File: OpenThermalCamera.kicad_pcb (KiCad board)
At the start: 2 copper layers, 26 x 20 mm, 23 parts, among them J1 Conn_ARM_JTAG_SWD_10, J2 DX07P024AJ1R1500, SW1 PB_Bootloader, U1 MLX90640, U2 TPS793333-EP, U3 STM32F042F6Px, U4 NUP2202

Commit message: First Rev3-C commit
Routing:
- net GND: track 82.0 -> 87.8 mm, vias 12 -> 14
- net +5V: track 46.0 -> 44.9 mm
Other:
- board text added: "OTC Rev3-C"
- board text removed: "OTC Rev3"

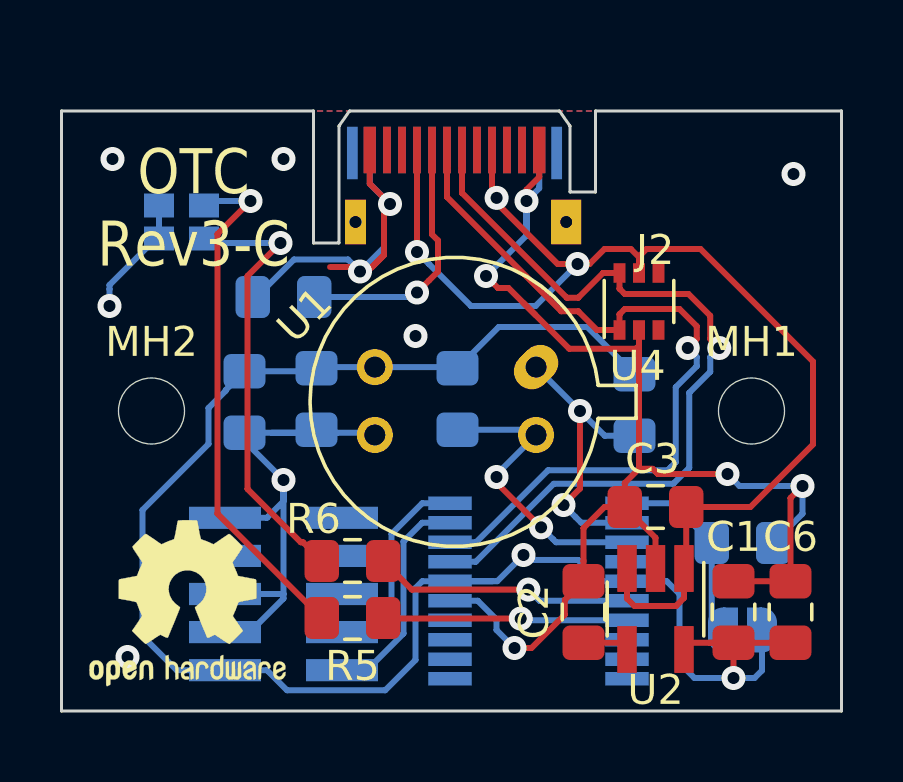
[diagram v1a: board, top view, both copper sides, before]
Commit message: Fixed reversible microusb footprint
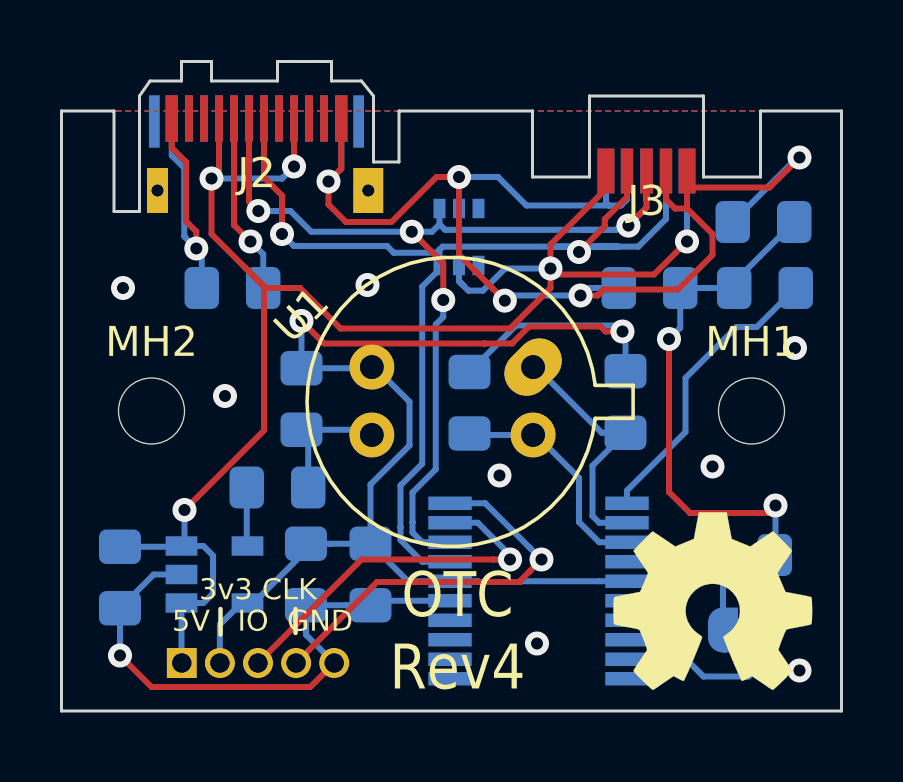
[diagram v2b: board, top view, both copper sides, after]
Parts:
- removed D1: LED_Dual_ACAC, LED_SMD:LED_Cree-PLCC4_2x2mm_CW
- added J3: micro5p_reversible, lib_fp:micro5p_reversible_edley_technology, F.Cu at (46.5, 28.0)
- C1, C2, C3, C6, U4: moved to B.Cu
- C4: value 1uF -> 10uF
- G1: value (none) -> Logo_Open_Hardware_Small; footprint Symbol:OSHW-Logo2_7.3x6mm_SilkScreen -> Symbol:OSHW-Symbol_6.7x6mm_SilkScreen
- J1: value Conn_ARM_JTAG_SWD_10 -> Conn_01x05_Female; footprint Connector_PinHeader_1.27mm:PinHeader_2x05_P1.27mm_Vertical_SMD -> Connector_PinHeader_1.27mm:PinHeader_1x05_P1.27mm_Vertical
- R1: value 10k -> 50k
- R5: value 10R -> 1k; moved to B.Cu
- R6: value 130R -> 1k; moved to B.Cu
- U2: value TPS793333-EP -> TPS79333-EP; footprint Package_TO_SOT_SMD:SOT-23-5_HandSoldering -> Package_TO_SOT_SMD:SOT-23-5; moved to B.Cu
- moved C3 18.0 mm to (28.9, 42.5), turned to 270 degrees
- moved R5 17.6 mm to (50.5, 32.9)
- moved G1 17.5 mm to (48.7, 43.4)
- moved U2 14.7 mm to (32.1, 42.5), turned to 0 degrees
- moved C1 14.3 mm to (35.1, 42.5), turned to 270 degrees
- moved C6 14.1 mm to (37.3, 42.5), turned to 270 degrees
- moved R6 13.1 mm to (49.8, 41.8)
- moved C4 11.7 mm to (46.6, 32.9), turned to 180 degrees
- moved C2 11.0 mm to (34.2, 39.5), turned to 0 degrees
- moved R1 10.7 mm to (50.4, 30.7), turned to 180 degrees
- moved J2 6.68 mm to (33.8, 28.4)
- moved U4 6.37 mm to (40.2, 31.2), turned to 270 degrees
- moved J1 4.10 mm to (31.0, 45.4), turned to 270 degrees
- moved C5 1.90 mm to (35.0, 36.6)
- moved R4 1.73 mm to (32.7, 32.9)
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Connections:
- C4 pad 1: +3V3 -> Net-(C4-Pad1)
- J1 pad 1: +3V3 -> +5V
- J1 pad 2: /SWDIO -> +3V3
- J1 pad 3: GND -> /SWDIO
- J2 pad A10: Net-(J2-PadA10) -> (no net)
- J2 pad A11: Net-(J2-PadA11) -> (no net)
- J2 pad A2: Net-(J2-PadA2) -> (no net)
- J2 pad A3: Net-(J2-PadA3) -> (no net)
- J2 pad A8: Net-(J2-PadA8) -> (no net)
- J2 pad B10: Net-(J2-PadB10) -> (no net)
- J2 pad B11: Net-(J2-PadB11) -> (no net)
- J2 pad B2: Net-(J2-PadB2) -> (no net)
- J2 pad B3: Net-(J2-PadB3) -> (no net)
- J2 pad B5: Net-(J2-PadB5) -> (no net)
- J2 pad B8: Net-(J2-PadB8) -> (no net)
- R1 pad 1: /BOOT0 -> Net-(C4-Pad1)
- R5 pad 1: Net-(D1-Pad1) -> Net-(C4-Pad1)
- R5 pad 2: /RED_LED -> /BOOT0
- R6 pad 1: /BLUE_LED -> Net-(C4-Pad1)
- R6 pad 2: Net-(D1-Pad4) -> Net-(R6-Pad2)
- SW1 pad 1: /BOOT0 -> Net-(R6-Pad2)
- U3 pad 10: Net-(U3-Pad10) -> (no net)
- U3 pad 11: Net-(U3-Pad11) -> (no net)
- U3 pad 12: Net-(U3-Pad12) -> (no net)
- U3 pad 13: Net-(U3-Pad13) -> (no net)
- U3 pad 14: Net-(U3-Pad14) -> (no net)
- U3 pad 4: Net-(U3-Pad4) -> (no net)
- U3 pad 6: /BLUE_LED -> (no net)
- U3 pad 7: /RED_LED -> (no net)
- U3 pad 8: Net-(U3-Pad8) -> (no net)
- U3 pad 9: Net-(U3-Pad9) -> (no net)
- U4 pad 3: Net-(U4-Pad3) -> (no net)
- U4 pad 4: Net-(U4-Pad4) -> (no net)
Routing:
- net Net-(D1-Pad1): track 17.4 -> 0.00 mm, vias 1 -> 0
- net Net-(C4-Pad1): track 0.00 -> 17.4 mm, vias 0 -> 2
- net +5V: track 44.9 -> 61.1 mm, vias 3 -> 5
- net Net-(D1-Pad4): track 14.7 -> 0.00 mm, vias 1 -> 0
- net /USB_N: track 27.9 -> 38.4 mm, vias 1 -> 2
- net /BLUE_LED: track 8.67 -> 0.00 mm, vias 1 -> 0
- net /USB_P: track 26.3 -> 34.7 mm, vias 1 -> 4
- net /RED_LED: track 8.16 -> 0.00 mm, vias 1 -> 0
- net +3V3: track 60.8 -> 54.1 mm
- net /SWDCLK: track 6.81 -> 13.4 mm, vias 0 -> 1
- net GND: track 87.8 -> 82.6 mm, vias 14 -> 15
- net /SWDIO: track 7.43 -> 12.4 mm, vias 0 -> 1
- net Net-(J2-PadA5): track 10.5 -> 6.05 mm
- net /BOOT0: track 6.43 -> 9.90 mm
- net /I2C_SCL: track 10.5 -> 7.61 mm, vias 2 -> 0
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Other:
- board size 26 x 20 mm -> 26 x 21.6 mm
- board text added: "3v3 CLK"
- board text added: "5V IO GND"
- board text added: "OTC Rev4"
- board text removed: "OTC Rev3-C"
